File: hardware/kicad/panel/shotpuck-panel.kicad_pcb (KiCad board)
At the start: 2 copper layers, 91 x 92.6 mm, 291 parts, among them J1_0 TYPE-C 6PFS 2JCB1.6-H6.7 IPX8, J1_1 TYPE-C 6PFS 2JCB1.6-H6.7 IPX8, J1_2 TYPE-C 6PFS 2JCB1.6-H6.7 IPX8, J1_3 TYPE-C 6PFS 2JCB1.6-H6.7 IPX8, J2_0 SWD pads, J2_1 SWD pads, J2_2 SWD pads, J2_3 SWD pads, Q1_0 DMN63D8LDW, Q1_1 DMN63D8LDW, Q1_2 DMN63D8LDW, Q1_3 DMN63D8LDW, Q2_0 DMN2004DWK, Q2_1 DMN2004DWK, Q2_2 DMN2004DWK, Q2_3 DMN2004DWK, U1_0 BMD-340-A-R, U1_1 BMD-340-A-R, U1_2 BMD-340-A-R, U1_3 BMD-340-A-R, U2_0 LSM6DSO32XTR, U2_1 LSM6DSO32XTR, U2_2 LSM6DSO32XTR, U2_3 LSM6DSO32XTR, U3_0 MCP73831T-2ACI/OT, U3_1 MCP73831T-2ACI/OT, U3_2 MCP73831T-2ACI/OT, U3_3 MCP73831T-2ACI/OT, U4_0 BQ29700DSER, U4_1 BQ29700DSER, U4_2 BQ29700DSER, U4_3 BQ29700DSER

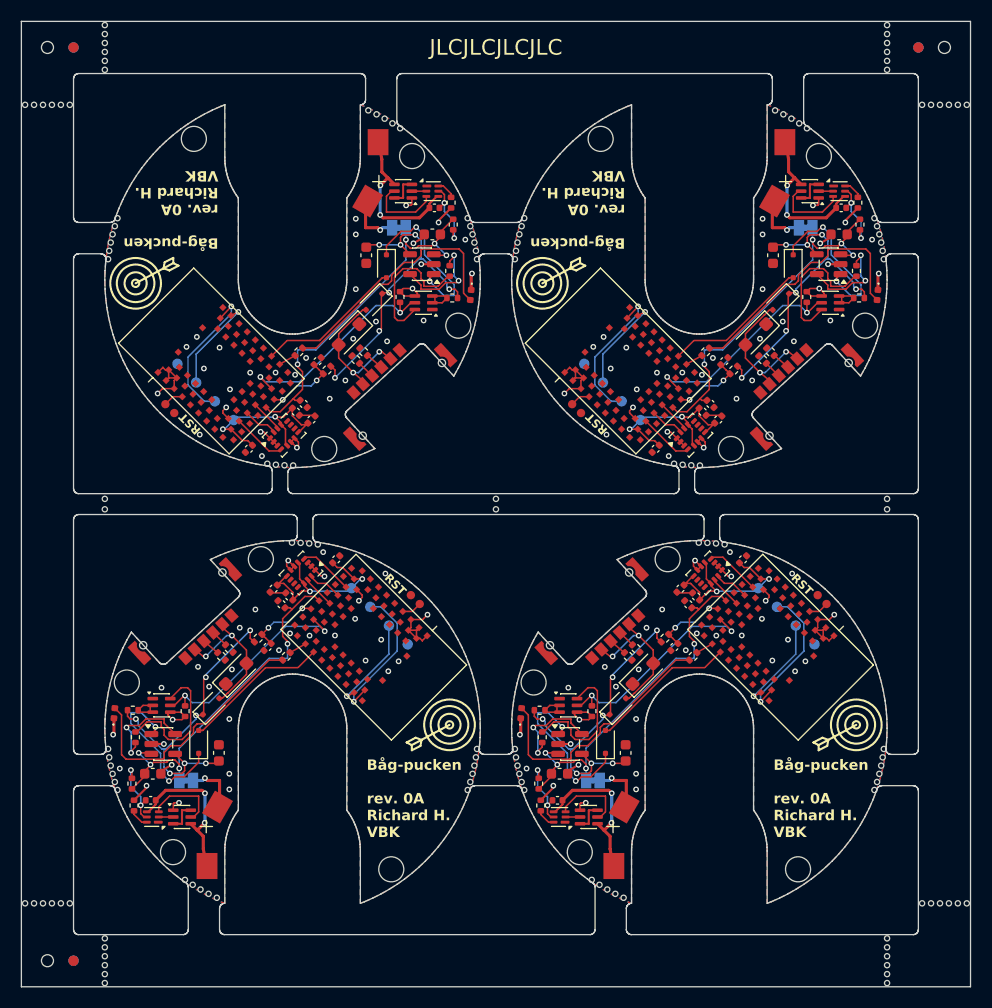
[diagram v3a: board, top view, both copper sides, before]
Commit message: Update HANDOVER and README with design adjustments and fixes
- Adjusted panel fiducial positions and tooling hole sizes to meet JLCPCB specifications.
- Moved U2 and associated components inward for better clearance from the top tab.
- Fixed outline slivers in the panel design to resolve DRC issues, ensuring all runs pass.
- Regenerated fabrication files, including updated gerbers and BOM, to reflect the latest changes.

Co-Authored-By: Claude Opus 5.5 <noreply@anthropic.com>
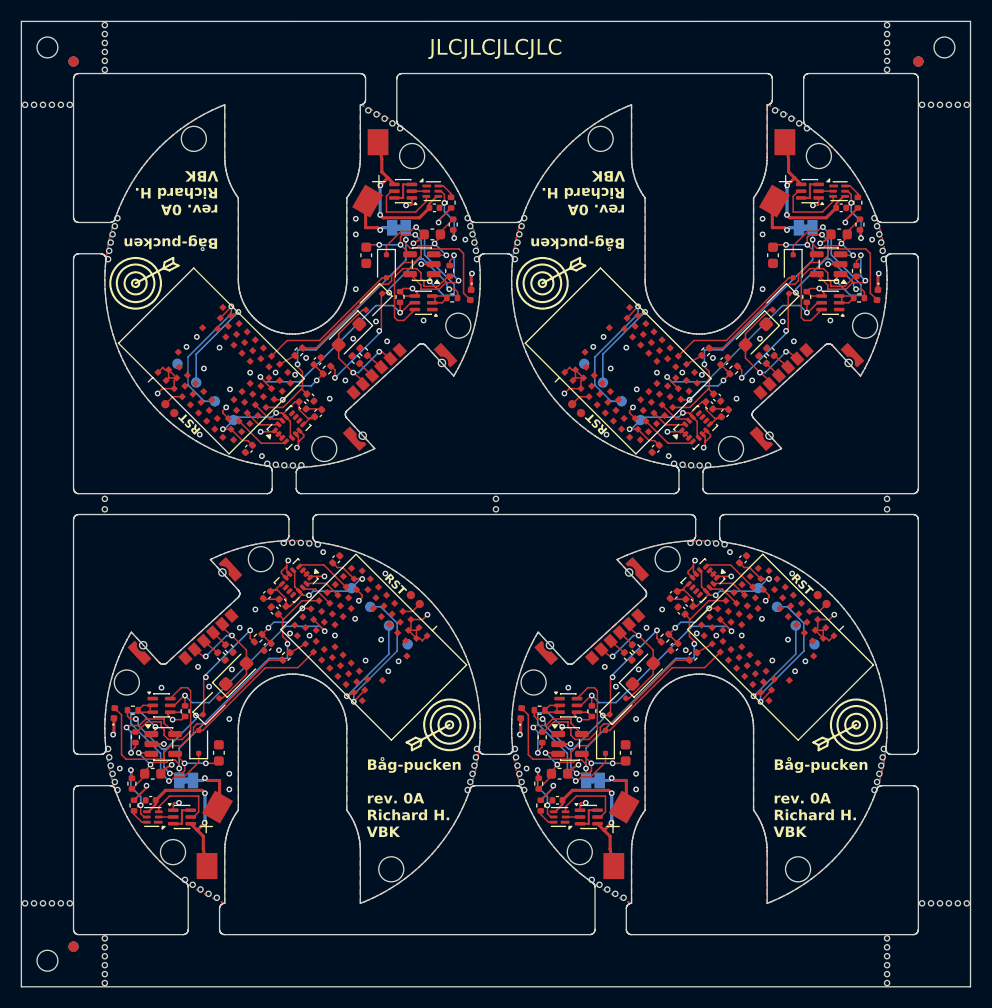
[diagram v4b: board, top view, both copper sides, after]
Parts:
- removed KiKit_MB_13_1, KiKit_MB_1_1, KiKit_MB_5_1, KiKit_MB_9_1: NPTH, NPTH
- added KiKit_MB_10_5: NPTH, NPTH, F.Cu at (131.4, 70.1)
- added KiKit_MB_11_1: NPTH, NPTH, F.Cu at (112.2, 93.7)
- added KiKit_MB_14_5: NPTH, NPTH, F.Cu at (170.4, 70.1)
- added KiKit_MB_15_1: NPTH, NPTH, F.Cu at (151.2, 93.7)
- added KiKit_MB_2_5: NPTH, NPTH, F.Cu at (126.6, 62.4)
- added KiKit_MB_3_1: NPTH, NPTH, F.Cu at (145.8, 38.9)
- added KiKit_MB_6_5: NPTH, NPTH, F.Cu at (165.6, 62.4)
- added KiKit_MB_7_1: NPTH, NPTH, F.Cu at (184.8, 38.9)
- moved KiKit_MB_19_2 75.0 mm to (186.0, 65.8)
- moved KiKit_MB_19_3 75.0 mm to (186.0, 66.8)
- moved KiKit_MB_17_2 37.5 mm to (111.0, 65.8)
- moved KiKit_MB_17_3 37.5 mm to (111.0, 66.8)
- moved KiKit_MB_18_2 37.5 mm to (148.5, 65.8)
- moved KiKit_MB_18_3 37.5 mm to (148.5, 66.8)
- moved KiKit_MB_1_2 14.8 mm to (136.3, 28.5)
- moved KiKit_MB_3_2 14.8 mm to (146.0, 39.6)
- moved KiKit_MB_5_2 14.8 mm to (175.3, 28.5)
- moved KiKit_MB_7_2 14.8 mm to (185.0, 39.6)
- moved KiKit_MB_13_2 14.8 mm to (160.7, 104.0)
- moved KiKit_MB_15_2 14.8 mm to (151.0, 92.9)
- moved KiKit_MB_11_2 14.8 mm to (112.0, 92.9)
- moved KiKit_MB_9_2 14.8 mm to (121.7, 104.0)
- moved KiKit_MB_11_3 14.7 mm to (111.7, 92.1)
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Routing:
- net Board_3-/GND: track 26.1 -> 27.2 mm
- net Board_1-/GND: track 26.1 -> 27.2 mm
- net Board_0-/GND: track 26.1 -> 27.2 mm
- net Board_2-/GND: track 26.1 -> 27.2 mm
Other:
- outline, holes or cut-outs redrawn

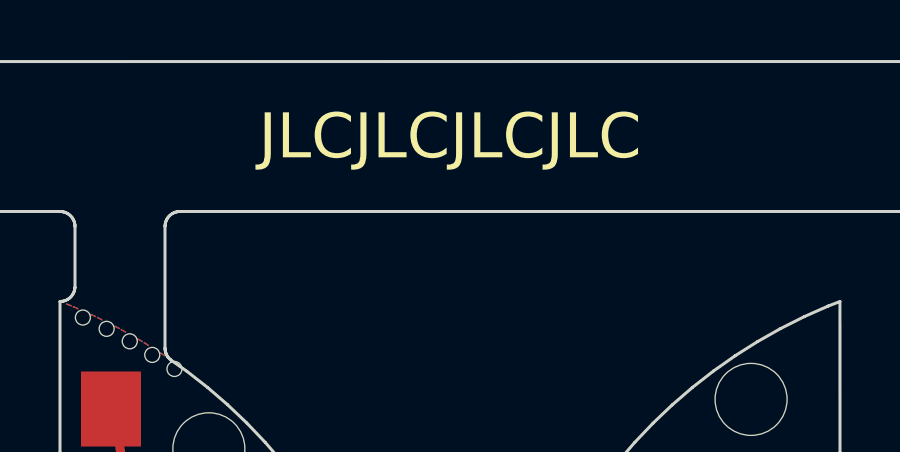
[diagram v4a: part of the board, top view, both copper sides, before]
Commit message: Update README and fabrication files for panel adjustments
- Modified drill export commands in README to include map generation for JLCPCB requirements.
- Updated README to clarify the drill map inclusion and fabrication process.
- Regenerated fabrication files, including updated gerbers and drill files, to reflect the latest design changes.

Co-Authored-By: Claude Opus 5.5 <noreply@anthropic.com>
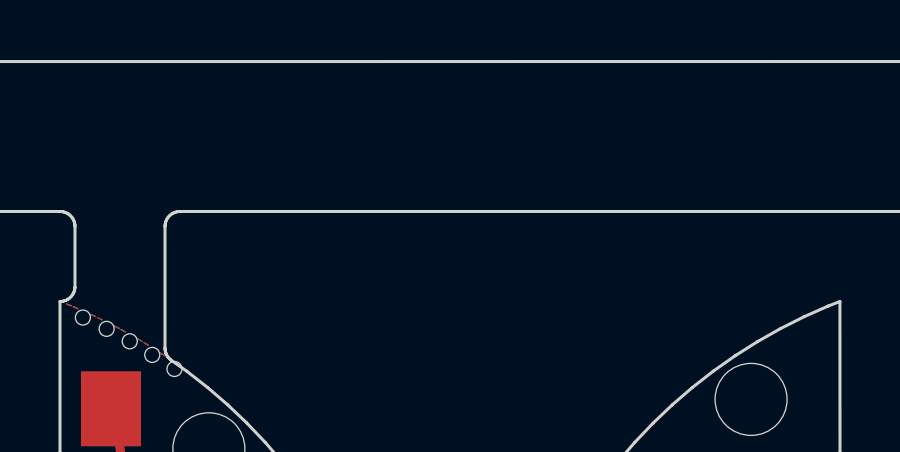
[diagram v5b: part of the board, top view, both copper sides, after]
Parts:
- removed KiKit_MB_12_1, KiKit_MB_16_1, KiKit_MB_4_1, KiKit_MB_8_1: NPTH, NPTH
- added KiKit_MB_13_1: NPTH, NPTH, F.Cu at (151.2, 93.7)
- added KiKit_MB_1_1: NPTH, NPTH, F.Cu at (145.8, 38.9)
- added KiKit_MB_5_1: NPTH, NPTH, F.Cu at (184.8, 38.9)
- added KiKit_MB_9_1: NPTH, NPTH, F.Cu at (112.2, 93.7)
- moved KiKit_MB_19_2 75.0 mm to (111.0, 65.8)
- moved KiKit_MB_19_3 75.0 mm to (111.0, 66.8)
- moved KiKit_MB_17_2 37.5 mm to (148.5, 66.8)
- moved KiKit_MB_17_3 37.5 mm to (148.5, 65.8)
- moved KiKit_MB_18_2 37.5 mm to (186.0, 65.8)
- moved KiKit_MB_18_3 37.5 mm to (186.0, 66.8)
- moved KiKit_MB_15_3 34.7 mm to (185.4, 91.4)
- moved KiKit_MB_15_4 34.7 mm to (185.3, 92.1)
- moved KiKit_MB_7_3 34.7 mm to (150.6, 41.2)
- moved KiKit_MB_7_4 34.7 mm to (150.7, 40.4)
- moved KiKit_MB_11_3 34.7 mm to (146.4, 91.4)
- moved KiKit_MB_11_4 34.7 mm to (146.3, 92.1)
- moved KiKit_MB_3_3 34.7 mm to (111.6, 41.2)
- moved KiKit_MB_3_4 34.7 mm to (111.7, 40.4)
- moved KiKit_MB_15_2 34.7 mm to (185.6, 90.6)
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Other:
- board text removed: "JLCJLCJLCJLC"

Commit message: Switch U2 to LSM6DSV32XTR and assemble 4 boards
- U2 is the LSM6DSV32XTR (C22461202): same pinout and land pattern, JLC
  footprint within 0.013 mm at 0 deg. Value fields, BOMs, pos file and
  schematic PDF updated; gerbers, drill files and CPL rows unchanged.
  Board DRC 0/0 with 0 parity issues, panel DRC 0/0, ERC unchanged.
- Firmware 0.2.2: accel.c ported to the LSM6DSV32X register map. ACTIVE
  runs at 480 Hz (captures 720 samples, ring 1329, motion guard 10
  samples), IDLE at 15 Hz. Rebuilt shotpuck_full.hex and update.bin.
- Sim ground truth 3360 Hz (7 x 480 Hz); results.txt regenerated, PASS.
- JLC order: PCBA qty 2 panels, BOM/CPL for the bottom-row copies only
  (gen_jlc.py ASSEMBLED_COPIES), so 4 boards are assembled.
- README, HANDOVER, PROTOCOL, VALIDATION, ORDER.md and the order zip
  updated.

Co-Authored-By: Claude Opus 5.5 <noreply@anthropic.com>
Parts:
- U2_0, U2_1, U2_2, U2_3: value LSM6DSO32XTR -> LSM6DSV32XTR
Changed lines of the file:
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@@
 			)
 		)
-		(property "Value" "LSM6DSO32XTR"
+		(property "Value" "LSM6DSV32XTR"
 			(at 0 2.2 225)
 			(unlocked yes)
@@
 			)
 		)
-		(property "Value" "LSM6DSO32XTR"
+		(property "Value" "LSM6DSV32XTR"
 			(at 0 2.2 45)
 			(unlocked yes)
@@
 			)
 		)
-		(property "Value" "LSM6DSO32XTR"
+		(property "Value" "LSM6DSV32XTR"
 			(at 0 2.2 45)
 			(unlocked yes)
@@
 			)
 		)
-		(property "Value" "LSM6DSO32XTR"
+		(property "Value" "LSM6DSV32XTR"
 			(at 0 2.2 225)
 			(unlocked yes)
